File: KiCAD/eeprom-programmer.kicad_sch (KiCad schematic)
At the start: 15 parts, among them J1 NUCLEO JP3, Q1 SI2305CD, SW1 ~{RST}, SW2 VDD select

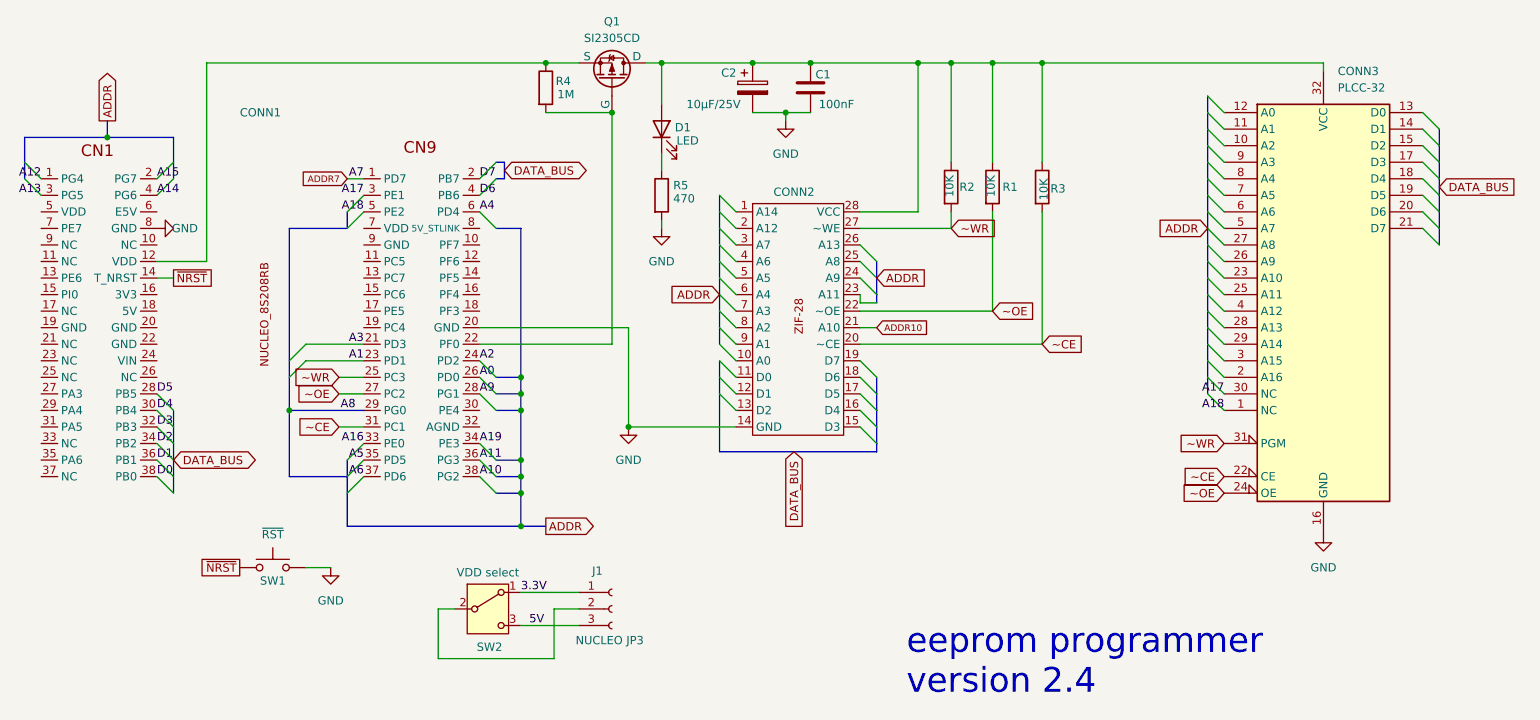
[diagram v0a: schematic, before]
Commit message: travail sur la version 3 du firmware qui ajoute le support pour la programmation des W25Q80DV
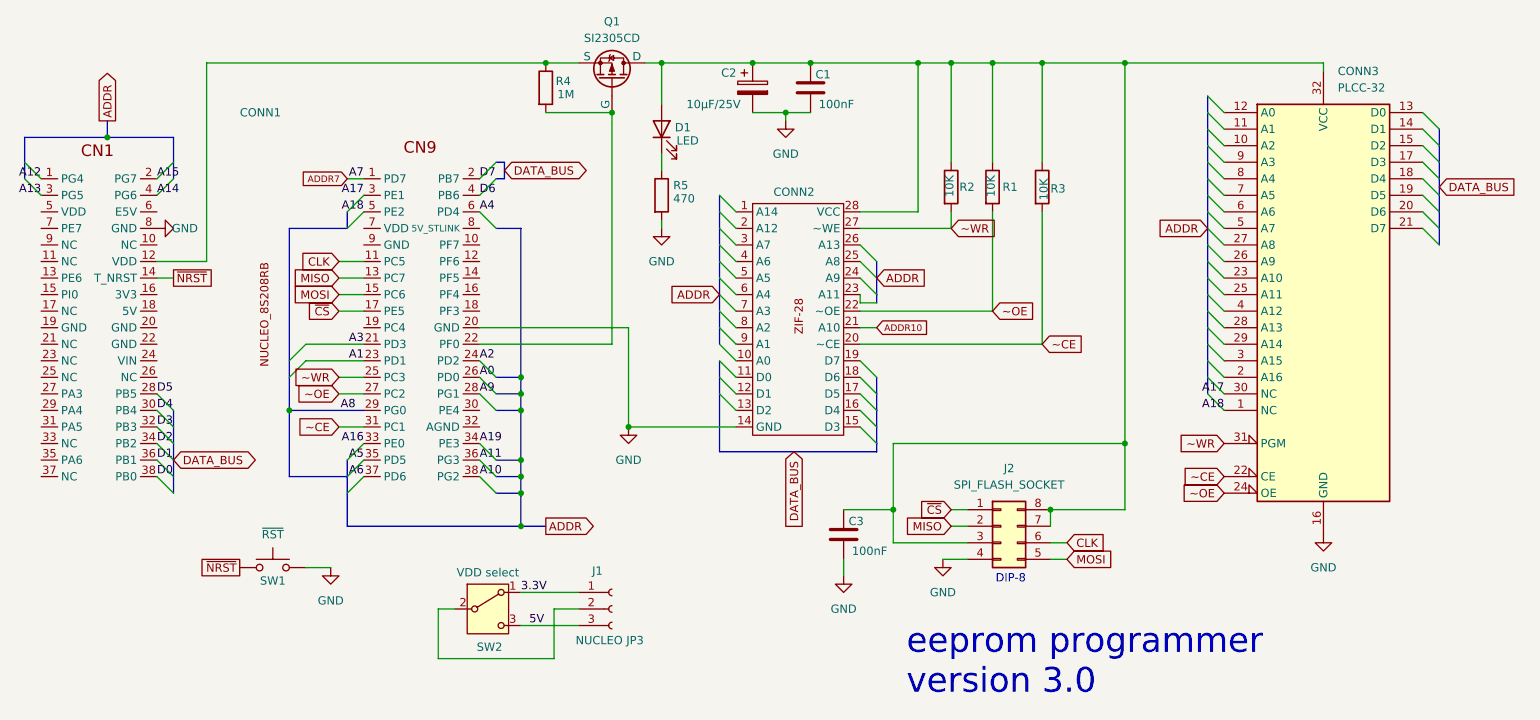
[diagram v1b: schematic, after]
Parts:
- added C3: 100nF, symbol Device:C
- added J2: SPI_FLASH_SOCKET, symbol Connector_Generic:Conn_02x04_Counter_Clockwise
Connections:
- net GND: now also C3.2, J2.4 (Pin_4)
- net at C1.1, C2.1, CONN2.28 (VCC)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: now also C3.1, J2.3 (Pin_3), J2.7 (Pin_7), J2.8 (Pin_8)
- net CLK: now reaches CONN1.11 (PC5)
- net CLK: now also J2.6 (Pin_6)
- net MISO: now reaches CONN1.13 (PC7)
- net MISO: now also J2.2 (Pin_2)
- net MOSI: now reaches CONN1.15 (PC6)
- net MOSI: now also J2.5 (Pin_5)
- net ~{CS}: now reaches CONN1.17 (PE5)
- net ~{CS}: now also J2.1 (Pin_1)
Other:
- note added: "DIP-8"
- note added: "eeprom programmer version 3.0"
- note removed: "eeprom programmer version 2.4"
